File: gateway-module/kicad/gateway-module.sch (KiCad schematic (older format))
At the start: 22 parts

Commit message: Communications Module PCB update
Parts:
- P1, P2: renamed from P?; footprint (none) -> SMA_coax:SMA_coax
- gave numbers to parts that had none: 20
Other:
- moved on the sheet: R2, R3, U1

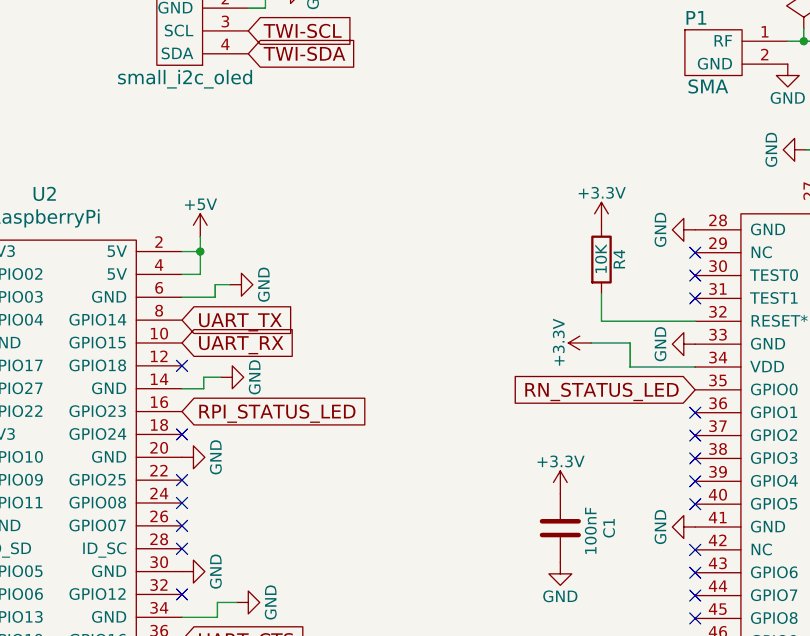
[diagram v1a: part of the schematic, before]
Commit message: Fixes #9 #8
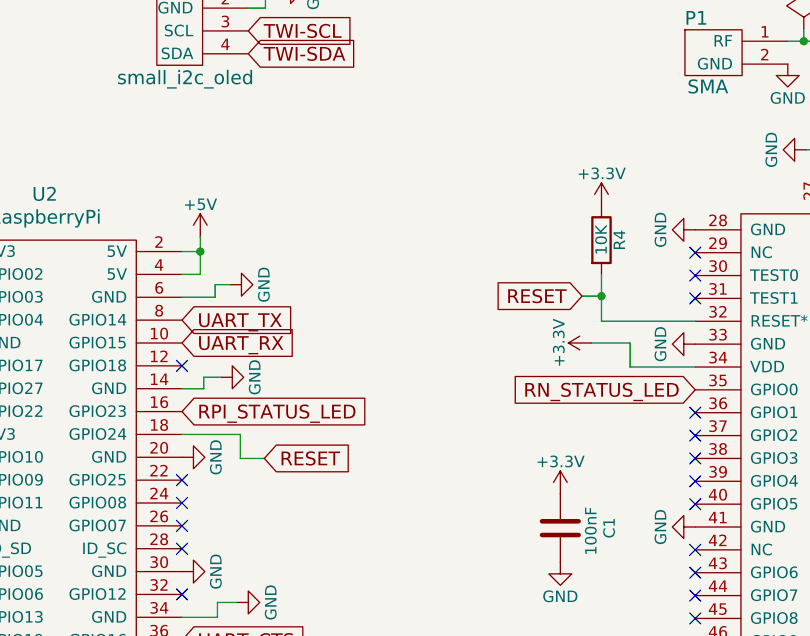
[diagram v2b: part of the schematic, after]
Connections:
- net RESET: now reaches R4.2, U3.32 (RESET*)
- net RESET: now also U2.18 (GPIO24)
- no-connect marks 47 -> 46
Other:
- moved on the sheet: R4
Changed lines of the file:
@@
 NoConn ~ 2940 4830
 NoConn ~ 2940 4730
-NoConn ~ 2940 4530
 NoConn ~ 2940 4230
 Text GLabel 6805 4935 2    60   Input ~ 0
@@
 L R R4
 U 1 1 5882996B
-P 4775 3765
-F 0 "R4" V 4855 3765 50  0000 C CNN
-F 1 "10K" V 4775 3765 50  0000 C CNN
-F 2 "0603_handsolder:0603_HandSoldering" V 4705 3765 30  0001 C CNN
-F 3 "" H 4775 3765 30  0000 C CNN
-	1    4775 3765
+P 4775 3680
+F 0 "R4" V 4855 3680 50  0000 C CNN
+F 1 "10K" V 4775 3680 50  0000 C CNN
+F 2 "0603_handsolder:0603_HandSoldering" V 4705 3680 30  0001 C CNN
+F 3 "" H 4775 3680 30  0000 C CNN
+	1    4775 3680
 	1    0    0    -1
 $EndComp
@@
 L +3.3V #PWR21
 U 1 1 58829971
-P 4775 3615
-F 0 "#PWR21" H 4775 3465 50  0001 C CNN
-F 1 "+3.3V" H 4775 3755 50  0000 C CNN
-F 2 "" H 4775 3615 60  0000 C CNN
-F 3 "" H 4775 3615 60  0000 C CNN
-	1    4775 3615
+P 4775 3530
+F 0 "#PWR21" H 4775 3380 50  0001 C CNN
+F 1 "+3.3V" H 4775 3670 50  0000 C CNN
+F 2 "" H 4775 3530 60  0000 C CNN
+F 3 "" H 4775 3530 60  0000 C CNN
+	1    4775 3530
 	1    0    0    -1
 $EndComp
@@
 	4900 4235 5185 4235
 Wire Wire Line
-	4775 3915 4775 4035
+	4775 3830 4775 4035
 Wire Wire Line
 	4775 4035 5185 4035
@@
 	6200 2750 6200 2810
 Connection ~ 6200 2810
+Text GLabel 4690 3925 0    60   Input ~ 0
+RESET
+Wire Wire Line
+	4690 3925 4775 3925
+Connection ~ 4775 3925
+Text GLabel 3300 4635 2    60   Input ~ 0
+RESET
+Wire Wire Line
+	2940 4530 3195 4530
+Wire Wire Line
+	3195 4530 3195 4635
+Wire Wire Line
+	3195 4635 3300 4635
 $EndSCHEMATC
